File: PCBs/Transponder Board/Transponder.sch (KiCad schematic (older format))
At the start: 21 parts, among them J1 Conn_01x02, J2 Conn_01x02, J3 Conn_01x02, J4 Conn_01x02, J5 Conn_01x02, J6 Conn_01x09, J7 Conn_01x02, U1 R-78E3.3-0.5, U2 MicroSDBreakout, U3 XBee-S2C

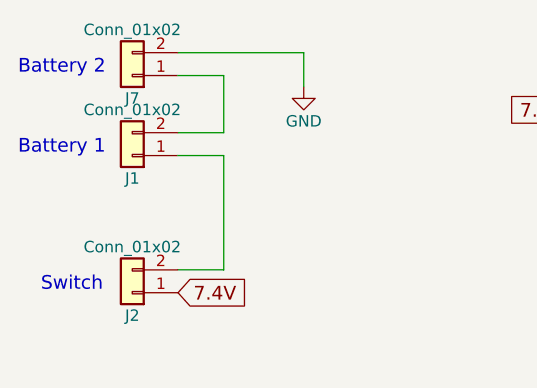
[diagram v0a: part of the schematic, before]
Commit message: Connector Changes
Flipped the transponder jst-ph connectors
Replaced the molex footprint on recovery with the correct one
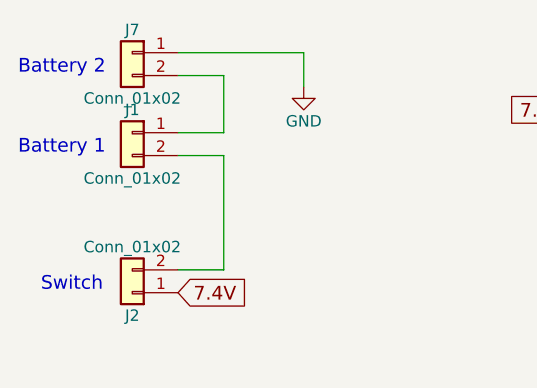
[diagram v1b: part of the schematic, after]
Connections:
- net GND: now also J7.1 (Pin_1); no longer J7.2 (Pin_2)
- net at J1.1 (Pin_1): now also J7.2 (Pin_2); no longer J2.2 (Pin_2)
- net at J1.2 (Pin_2): now also J2.2 (Pin_2); no longer J7.1 (Pin_1)
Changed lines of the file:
@@
 	1    0    0    -1
 $EndComp
-Wire Wire Line
-	1250 5950 1250 6250
-Connection ~ 1250 6050
 $Comp
 L XBee-S2C U3
@@
 Text GLabel 6850 4150 0    60   Input ~ 0
 SLK
-Wire Wire Line
-	6850 4050 6550 4050
-Wire Wire Line
-	6550 4050 6550 4300
 Text GLabel 7850 3850 2    60   Input ~ 0
 MISO
@@
 	1    0    0    -1
 $EndComp
-Wire Wire Line
-	3550 950  3550 900
-Wire Wire Line
-	3300 900  3800 900
-Wire Wire Line
-	3550 1250 3550 1350
 Text GLabel 3300 900  0    60   Input ~ 0
 7.4V
-Connection ~ 3550 900
 $Comp
 L C C2
@@
 	1    0    0    -1
 $EndComp
-Wire Wire Line
-	5150 950  5150 900
-Connection ~ 5150 900
 $Comp
 L GND #PWR05
@@
 	1    0    0    -1
 $EndComp
-Wire Wire Line
-	5150 1350 5150 1250
 Text GLabel 7900 1900 0    60   Input ~ 0
 XBEE-DOUT
@@
 	1    0    0    -1
 $EndComp
-Wire Wire Line
-	6050 2150 6300 2150
-Wire Wire Line
-	6300 2150 6300 2500
-Wire Wire Line
-	6300 2800 6300 3050
-Wire Wire Line
-	6300 2950 7700 2950
-Wire Wire Line
-	7700 2950 7700 2000
-Wire Wire Line
-	7700 2000 7900 2000
-Connection ~ 6300 2950
 $Comp
 L GND #PWR06
@@
 	1    0    0    -1
 $EndComp
-Wire Wire Line
-	6300 3500 6300 3350
 $Comp
 L GND #PWR07
@@
 	1    0    0    -1
 $EndComp
-Wire Wire Line
-	7800 2900 7800 2700
-Wire Wire Line
-	7800 2700 7900 2700
 Text GLabel 1550 1700 2    60   Input ~ 0
 7.4V
@@
 L Conn_01x02 J1
 U 1 1 5AA89FA6
-P 1350 1100
-F 0 "J1" H 1350 1200 50  0000 C CNN
-F 1 "Conn_01x02" H 1350 900 50  0000 C CNN
-F 2 "Connectors_JST:JST_PH_B2B-PH-K_02x2.00mm_Straight" H 1350 1100 50  0001 C CNN
-F 3 "" H 1350 1100 50  0001 C CNN
-	1    1350 1100
-	-1   0    0    1
+P 1350 1000
+F 0 "J1" H 1350 1100 50  0000 C CNN
+F 1 "Conn_01x02" H 1350 800 50  0000 C CNN
+F 2 "Connectors_JST:JST_PH_B2B-PH-K_02x2.00mm_Straight" H 1350 1000 50  0001 C CNN
+F 3 "" H 1350 1000 50  0001 C CNN
+	1    1350 1000
+	-1   0    0    -1
 $EndComp
 $Comp
@@
 	-1   0    0    1
 $EndComp
-Wire Wire Line
-	1550 650  2100 650
-Wire Wire Line
-	2100 650  2100 800
 $Comp
 L Conn_01x02 J3
@@
 	1    0    0    -1
 $EndComp
-Wire Wire Line
-	2600 5400 3650 5400
-Connection ~ 3600 5400
-Wire Wire Line
-	2600 5500 3350 5500
-Connection ~ 3300 5500
-Wire Wire Line
-	2600 5600 3050 5600
-Connection ~ 3000 5600
 $Comp
 L GND #PWR09
@@
 Text GLabel 5500 900  2    60   Input ~ 0
 3.3V
-Wire Wire Line
-	4900 900  5500 900
 Text GLabel 6400 1800 0    60   Input ~ 0
 3.3V
@@
 	1    0    0    -1
 $EndComp
-Wire Wire Line
-	5850 5900 5850 5850
-Wire Wire Line
-	5850 5850 5950 5850
 Text GLabel 5950 5750 0    60   Input ~ 0
 5V
@@
 	1    0    0    -1
 $EndComp
-Wire Wire Line
-	5300 5900 5300 5550
-Wire Wire Line
-	5300 5550 5950 5550
 Text GLabel 5950 5350 0    60   Input ~ 0
 LCD_D4
@@
 Text GLabel 2600 4700 2    60   Input ~ 0
 LCD_H/L_RS
-Wire Wire Line
-	1550 1100 1750 1100
-Wire Wire Line
-	1750 1100 1750 1600
-Wire Wire Line
-	1750 1600 1550 1600
 Text Notes 850  1100 0    60   ~ 0
 Battery 1
@@
 	1    0    0    -1
 $EndComp
-Wire Wire Line
-	6400 1800 7900 1800
-Wire Wire Line
-	6550 1850 6550 1800
-Connection ~ 6550 1800
-Wire Wire Line
-	6850 1850 6850 1800
-Connection ~ 6850 1800
-Wire Wire Line
-	7150 1850 7150 1800
-Connection ~ 7150 1800
 $Comp
 L GND #PWR014
@@
 Text GLabel 4150 4100 2    60   Input ~ 0
 XBEE-DOUT
-Wire Wire Line
-	2600 4100 3450 4100
 $Comp
 L Conn_01x02 J7
 U 1 1 5AC4138A
-P 1350 750
-F 0 "J7" H 1350 850 50  0000 C CNN
-F 1 "Conn_01x02" H 1350 550 50  0000 C CNN
-F 2 "Connectors_JST:JST_PH_B2B-PH-K_02x2.00mm_Straight" H 1350 750 50  0001 C CNN
-F 3 "" H 1350 750 50  0001 C CNN
-	1    1350 750
-	-1   0    0    1
+P 1350 650
+F 0 "J7" H 1350 750 50  0000 C CNN
+F 1 "Conn_01x02" H 1350 450 50  0000 C CNN
+F 2 "Connectors_JST:JST_PH_B2B-PH-K_02x2.00mm_Straight" H 1350 650 50  0001 C CNN
+F 3 "" H 1350 650 50  0001 C CNN
+	1    1350 650
+	-1   0    0    -1
 $EndComp
 Text Notes 850  750  0    60   ~ 0
 Battery 2
 Wire Wire Line
+	1250 5950 1250 6250
+Connection ~ 1250 6050
+Wire Wire Line
+	6850 4050 6550 4050
+Wire Wire Line
+	6550 4050 6550 4300
+Wire Wire Line
+	3550 950  3550 900
+Wire Wire Line
+	3300 900  3800 900
+Wire Wire Line
+	3550 1250 3550 1350
+Connection ~ 3550 900
+Wire Wire Line
+	5150 950  5150 900
+Connection ~ 5150 900
+Wire Wire Line
+	5150 1350 5150 1250
+Wire Wire Line
+	6050 2150 6300 2150
+Wire Wire Line
+	6300 2150 6300 2500
+Wire Wire Line
+	6300 2800 6300 3050
+Wire Wire Line
+	6300 2950 7700 2950
+Wire Wire Line
+	7700 2950 7700 2000
+Wire Wire Line
+	7700 2000 7900 2000
+Connection ~ 6300 2950
+Wire Wire Line
+	6300 3500 6300 3350
+Wire Wire Line
+	7800 2900 7800 2700
+Wire Wire Line
+	7800 2700 7900 2700
+Wire Wire Line
+	2600 5400 3650 5400
+Connection ~ 3600 5400
+Wire Wire Line
+	2600 5500 3350 5500
+Connection ~ 3300 5500
+Wire Wire Line
+	2600 5600 3050 5600
+Connection ~ 3000 5600
+Wire Wire Line
+	4900 900  5500 900
+Wire Wire Line
+	5850 5900 5850 5850
+Wire Wire Line
+	5850 5850 5950 5850
+Wire Wire Line
+	5300 5900 5300 5550
+Wire Wire Line
+	5300 5550 5950 5550
+Wire Wire Line
+	6400 1800 7900 1800
+Wire Wire Line
+	6550 1850 6550 1800
+Connection ~ 6550 1800
+Wire Wire Line
+	6850 1850 6850 1800
+Connection ~ 6850 1800
+Wire Wire Line
+	7150 1850 7150 1800
+Connection ~ 7150 1800
+Wire Wire Line
+	2600 4100 3450 4100
+Wire Wire Line
 	1550 1000 1750 1000
 Wire Wire Line
+	1750 1600 1550 1600
+Wire Wire Line
+	1550 1100 1750 1100
+Wire Wire Line
+	1750 1100 1750 1600
+Wire Wire Line
+	1550 650  2100 650
+Wire Wire Line
+	2100 650  2100 800
+Wire Wire Line
 	1750 1000 1750 750
